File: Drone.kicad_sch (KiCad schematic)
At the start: 46 parts, among them J1 USB_C_Receptacle_USB2.0_16P, J2 Conn_01x02_Pin, J3 Conn_01x06_Socket, J4 Conn_01x06_Socket, Q1 AO3401A, SW1 SW_DPDT_x2, SW2 RST, SW3 BOOT, U1 TP4056-42-ESOP8, U2 MIC5219-3.3YM5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

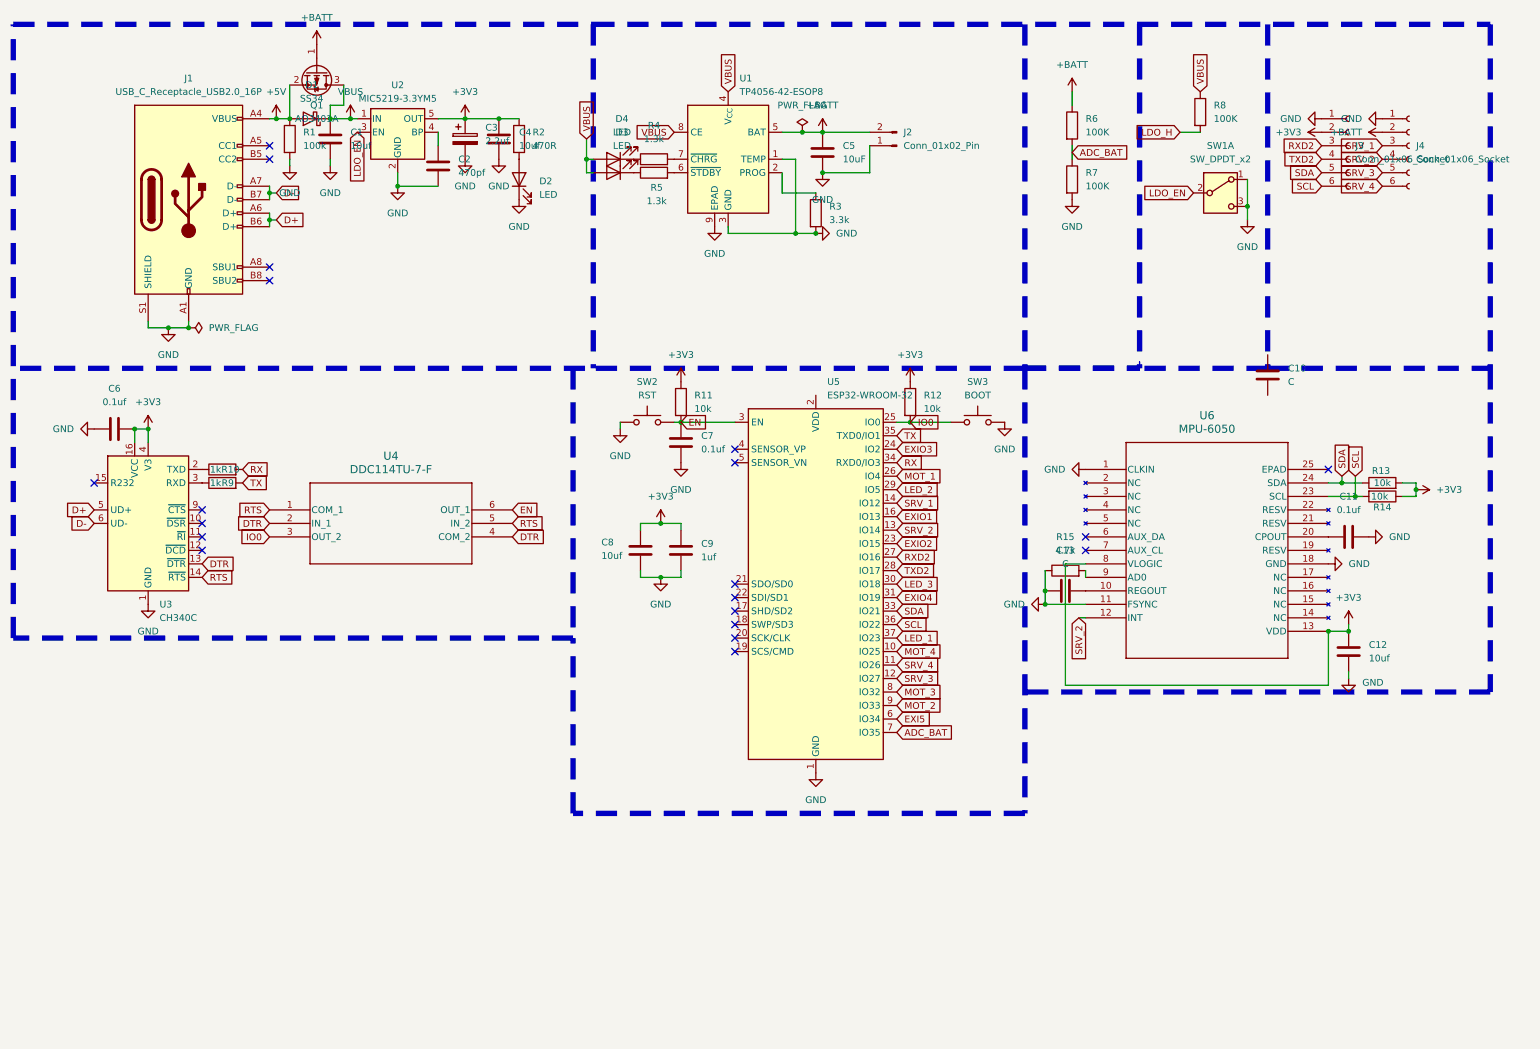
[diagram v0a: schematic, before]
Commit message: added n channel mosfets
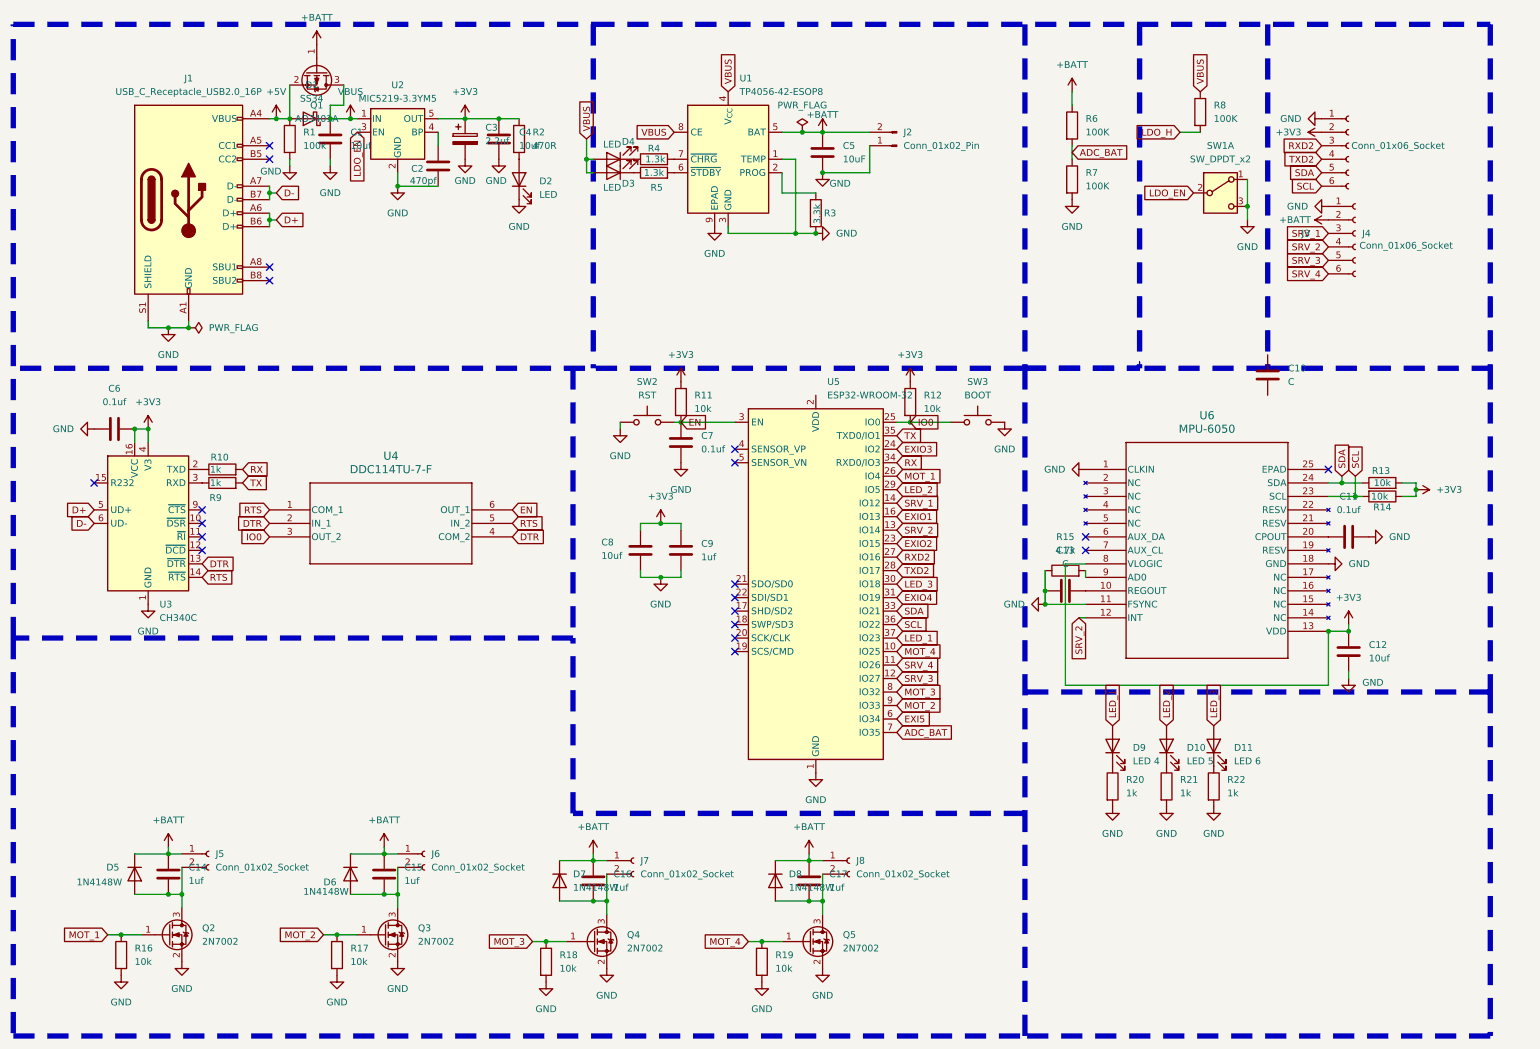
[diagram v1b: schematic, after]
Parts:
- added C14, C15, C16, C17: 1uf, symbol Device:C
- added D10: LED 5, symbol Device:LED
- added D11: LED 6, symbol Device:LED
- added D5, D6, D7, D8: 1N4148W, Diode_SMD:D_SOD-123, symbol Diode:1N4148W
- added D9: LED 4, symbol Device:LED
- added J5, J6, J7, J8: Conn_01x02_Socket, symbol Connector:Conn_01x02_Socket
- added Q2, Q3, Q4, Q5: 2N7002, Package_TO_SOT_SMD:SOT-23, symbol Transistor_FET:2N7002
- added R16, R17, R18, R19: 10k, symbol Device:R
- added R20, R21, R22: 1k, symbol Device:R
- C1, C10, C11, C12, C13, C2, C3, C4, C5, C6, C7, C8: footprint (none) -> Capacitor_SMD:C_0603_1608Metric
- C9: footprint 10uf -> Capacitor_SMD:C_0603_1608Metric
- D1: footprint Diode_SMD:D_SMA -> Diode_SMD:D_0603_1608Metric
- D2, D3, D4: footprint (none) -> LED_SMD:LED_0603_1608Metric
- J1: footprint (none) -> Connector_USB:USB_C_Receptacle_HCTL_HC-TYPE-C-16P-01A
- J2: footprint (none) -> Connector_PinHeader_2.54mm:PinHeader_1x06_P2.54mm_Vertical
- J3, J4: footprint (none) -> Connector_PinSocket_2.54mm:PinSocket_1x06_P2.54mm_Vertical
- R1, R10, R11, R12, R13, R14, R15, R2, R3, R4, R5, R6, R7, R8, R9: footprint (none) -> Resistor_SMD:R_0603_1608Metric
- U4: footprint SOT_363_DIO -> DDC:SOT_363_DIO
- U6: footprint QFN24_4X4X0P9-0P5_TDK -> footprints:QFN24_4X4X0P9-0P5_TDK
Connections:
- net +BATT: now also C14.1, C15.1, C16.1, C17.1, D5.1 (K), D6.1 (K), D7.1 (K), D8.1 (K), J5.1 (Pin_1), J6.1 (Pin_1), J7.1 (Pin_1), J8.1 (Pin_1)
- net GND: now also Q2.2 (S), Q3.2 (S), Q4.2 (S), Q5.2 (S), R16.2, R17.2, R18.2, R19.2, R20.2, R21.2, R22.2
- net LED_1: now also D9.2 (A)
- net LED_2: now also D10.2 (A)
- net LED_3: now also D11.2 (A)
- net MOT_1: now also Q2.1 (G), R16.1
- net MOT_2: now also Q3.1 (G), R17.1
- net MOT_3: now also Q4.1 (G), R18.1
- net MOT_4: now also Q5.1 (G), R19.1
- new net: D11.1 (K), R22.1
- new net: C17.2, D8.2 (A), J8.2 (Pin_2), Q5.3 (D)
- new net: D10.1 (K), R21.1
- new net: C14.2, D5.2 (A), J5.2 (Pin_2), Q2.3 (D)
- new net: C16.2, D7.2 (A), J7.2 (Pin_2), Q4.3 (D)
- new net: C15.2, D6.2 (A), J6.2 (Pin_2), Q3.3 (D)
- new net: D9.1 (K), R20.1
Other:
- moved on the sheet: J4

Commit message: V1 of PCB
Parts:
- removed C10: C, Capacitor_SMD:C_0603_1608Metric, symbol Device:C
- C14, C15, C16, C17: footprint (none) -> Capacitor_SMD:C_0603_1608Metric
- D10, D11, D9: footprint (none) -> LED_SMD:LED_0603_1608Metric
- J2: footprint Connector_PinHeader_2.54mm:PinHeader_1x06_P2.54mm_Vertical -> Connector_PinHeader_2.54mm:PinHeader_1x02_P2.54mm_Vertical
- J3, J4: footprint Connector_PinSocket_2.54mm:PinSocket_1x06_P2.54mm_Vertical -> Connector_PinHeader_2.54mm:PinHeader_1x06_P2.54mm_Vertical
- J5, J6, J7, J8: footprint (none) -> Connector_PinHeader_2.54mm:PinHeader_1x02_P2.54mm_Vertical
- R16, R17, R18, R19, R20, R21, R22: footprint (none) -> Resistor_SMD:R_0603_1608Metric
- SW1, SW2, SW3: footprint (none) -> Button_Switch_THT:SW_PUSH_6mm
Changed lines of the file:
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@@
 			)
 		)
-		(property "Footprint" ""
+		(property "Footprint" "LED_SMD:LED_0603_1608Metric"
 			(at 236.22 146.05 0)
 			(effects
@@
 			)
 		)
-		(property "Footprint" "Connector_PinSocket_2.54mm:PinSocket_1x06_P2.54mm_Vertical"
+		(property "Footprint" "Connector_PinHeader_2.54mm:PinHeader_1x06_P2.54mm_Vertical"
 			(at 262.89 49.53 0)
 			(effects
@@
 			)
 		)
-		(property "Footprint" ""
+		(property "Footprint" "LED_SMD:LED_0603_1608Metric"
 			(at 227.33 146.05 0)
 			(effects
@@
 	)
 	(symbol
-		(lib_id "Device:C")
-		(at 246.38 76.2 0)
-		(unit 1)
-		(exclude_from_sim no)
-		(in_bom yes)
-		(on_board yes)
-		(dnp no)
-		(fields_autoplaced yes)
-		(property "Reference" "C10"
-			(at 250.19 74.9299 0)
-			(effects
-				(font
-					(size 1.27 1.27)
-				)
-				(justify left)
-			)
-		)
-		(property "Value" "C"
-			(at 250.19 77.4699 0)
-			(effects
-				(font
-					(size 1.27 1.27)
-				)
-				(justify left)
-			)
-		)
-		(property "Footprint" "Capacitor_SMD:C_0603_1608Metric"
-			(at 247.3452 80.01 0)
-			(effects
-				(font
-					(size 1.27 1.27)
-				)
-				(hide yes)
-			)
-		)
-		(property "Datasheet" "~"
-			(at 246.38 76.2 0)
-			(effects
-				(font
-					(size 1.27 1.27)
-				)
-				(hide yes)
-			)
-		)
-		(property "Description" "Unpolarized capacitor"
-			(at 246.38 76.2 0)
-			(effects
-				(font
-					(size 1.27 1.27)
-				)
-				(hide yes)
-			)
-		)
-		(pin "1"
-		)
-		(pin "2"
-		)
-		(instances
-			(project ""
-				(path "/9d1f16d7-7b1e-4db7-b67a-82fae88f8320"
-					(reference "C10")
-					(unit 1)
-				)
-			)
-		)
-	)
-	(symbol
 		(lib_id "power:PWR_FLAG")
 		(at 158.75 30.48 0)
@@
 			)
 		)
-		(property "Footprint" ""
+		(property "Footprint" "Resistor_SMD:R_0603_1608Metric"
 			(at 149.352 186.69 90)
 			(effects
@@
 			)
 		)
-		(property "Footprint" ""
+		(property "Footprint" "Resistor_SMD:R_0603_1608Metric"
 			(at 225.552 153.67 90)
 			(effects
@@
 			)
 		)
-		(property "Footprint" ""
+		(property "Footprint" "Button_Switch_THT:SW_PUSH_6mm"
 			(at 129.54 80.01 0)
 			(effects
@@
 			)
 		)
-		(property "Footprint" ""
+		(property "Footprint" "Resistor_SMD:R_0603_1608Metric"
 			(at 234.442 153.67 90)
 			(effects
@@
 			)
 		)
-		(property "Footprint" "Connector_PinHeader_2.54mm:PinHeader_1x06_P2.54mm_Vertical"
+		(property "Footprint" "Connector_PinHeader_2.54mm:PinHeader_1x02_P2.54mm_Vertical"
 			(at 176.53 33.02 0)
 			(effects
@@
 			)
 		)
-		(property "Footprint" ""
+		(property "Footprint" "Connector_PinHeader_2.54mm:PinHeader_1x02_P2.54mm_Vertical"
 			(at 167.64 167.64 0)
 			(effects
@@
 			)
 		)
-		(property "Footprint" ""
+		(property "Footprint" "Resistor_SMD:R_0603_1608Metric"
 			(at 28.702 185.42 90)
 			(effects
@@
 			)
 		)
-		(property "Footprint" ""
+		(property "Footprint" "Capacitor_SMD:C_0603_1608Metric"
 			(at 40.3352 173.99 0)
 			(effects
@@
 			)
 		)
-		(property "Footprint" ""
+		(property "Footprint" "Resistor_SMD:R_0603_1608Metric"
 			(at 108.712 186.69 90)
 			(effects
@@
 			)
 		)
-		(property "Footprint" ""
+		(property "Footprint" "Connector_PinHeader_2.54mm:PinHeader_1x02_P2.54mm_Vertical"
 			(at 127 167.64 0)
 			(effects
@@
 			)
 		)
-		(property "Footprint" ""
+		(property "Footprint" "Button_Switch_THT:SW_PUSH_6mm"
 			(at 237.49 41.91 0)
 			(effects
@@
 			)
 		)
-		(property "Footprint" ""
+		(property "Footprint" "Capacitor_SMD:C_0603_1608Metric"
 			(at 160.9852 175.26 0)
 			(effects
@@
 			)
 		)
-		(property "Footprint" ""
+		(property "Footprint" "Resistor_SMD:R_0603_1608Metric"
 			(at 69.342 185.42 90)
 			(effects
@@
 			)
 		)
-		(property "Footprint" ""
+		(property "Footprint" "Connector_PinHeader_2.54mm:PinHeader_1x02_P2.54mm_Vertical"
 			(at 46.99 166.37 0)
 			(effects
@@
 			)
 		)
-		(property "Footprint" ""
+		(property "Footprint" "Button_Switch_THT:SW_PUSH_6mm"
 			(at 191.77 80.01 0)
 			(effects
@@
 			)
 		)
-		(property "Footprint" ""
+		(property "Footprint" "Resistor_SMD:R_0603_1608Metric"
 			(at 215.392 153.67 90)
 			(effects
@@
 			)
 		)
-		(property "Footprint" "Connector_PinSocket_2.54mm:PinSocket_1x06_P2.54mm_Vertical"
+		(property "Footprint" "Connector_PinHeader_2.54mm:PinHeader_1x06_P2.54mm_Vertical"
 			(at 261.62 33.02 0)
 			(effects
@@
 			)
 		)
-		(property "Footprint" ""
+		(property "Footprint" "Capacitor_SMD:C_0603_1608Metric"
 			(at 120.3452 175.26 0)
 			(effects
@@
 			)
 		)
-		(property "Footprint" ""
+		(property "Footprint" "Capacitor_SMD:C_0603_1608Metric"
 			(at 80.9752 173.99 0)
 			(effects
@@
 			)
 		)
-		(property "Footprint" ""
+		(property "Footprint" "Connector_PinHeader_2.54mm:PinHeader_1x02_P2.54mm_Vertical"
 			(at 87.63 166.37 0)
 			(effects
@@
 			)
 		)
-		(property "Footprint" ""
+		(property "Footprint" "LED_SMD:LED_0603_1608Metric"
 			(at 217.17 146.05 0)
 			(effects
